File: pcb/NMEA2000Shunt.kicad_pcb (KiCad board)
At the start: 2 copper layers, 87.3 x 28.3 mm, 26 parts, among them IC101 ATTINY3224-SS, K101 Battery, P101 Temp1, P102 Prog, P103 CAN, P105 OLED, U101 MCP2515, U102 TJA1050, U103 NCP1117ST50T3G, U104 INA219-module, X101 8MHz

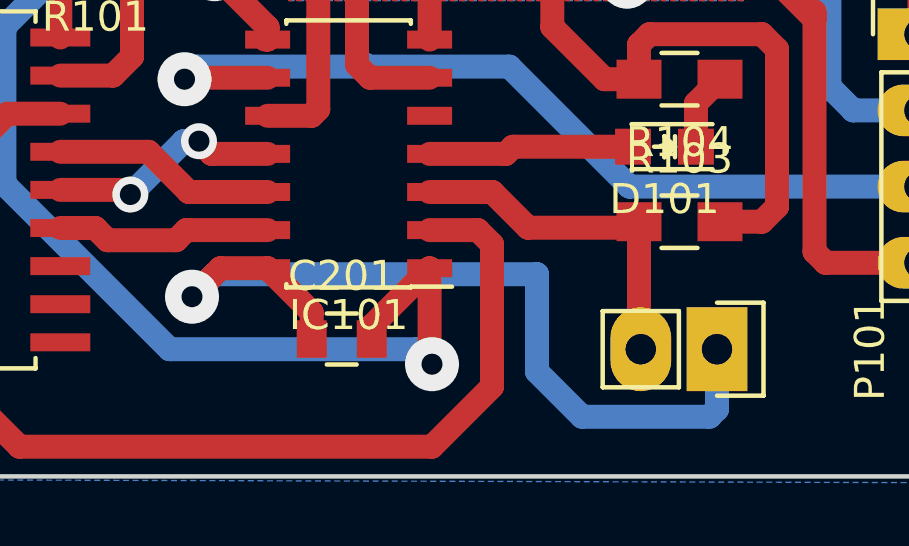
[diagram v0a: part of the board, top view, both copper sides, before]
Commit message: Working version tested with Cansocket and canboat
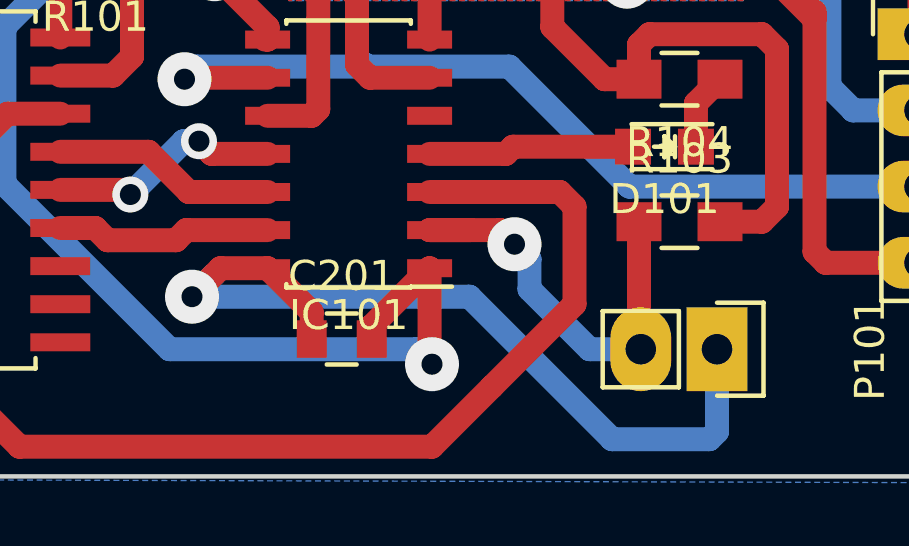
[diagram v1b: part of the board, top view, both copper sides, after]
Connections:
- IC101 pad 2: CANCS -> TEMP1
- IC101 pad 3: TEMP1 -> CANCS
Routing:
- net CANCS: track 37.3 -> 42.5 mm
- net TEMP1: track 11.8 -> 15.8 mm, vias 0 -> 1
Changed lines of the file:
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@@
     (links 65)
     (no_connects 0)
-    (area 105.894999 108.738999 193.365001 137.239001)
+    (area 84.68345 95.464 194.015001 272.896001)
     (thickness 1.6)
     (drawings 12)
-    (tracks 268)
+    (tracks 273)
     (zones 0)
     (modules 26)
@@
       (net 11 5V))
     (pad 2 smd rect (at -2.7 -2.54 180) (size 1.5 0.6) (layers F.Cu F.Paste F.Mask)
+      (net 23 TEMP1))
+    (pad 3 smd rect (at -2.7 -1.27 180) (size 1.5 0.6) (layers F.Cu F.Paste F.Mask)
       (net 3 CANCS))
-    (pad 3 smd rect (at -2.7 -1.27 180) (size 1.5 0.6) (layers F.Cu F.Paste F.Mask)
-      (net 23 TEMP1))
     (pad 4 smd rect (at -2.7 0 180) (size 1.5 0.6) (layers F.Cu F.Paste F.Mask)
       (net 21 LED))
@@
   (segment (start 143.934 127.424) (end 146.56 127.424) (width 0.8) (layer F.Cu) (net 2) (status 20))
   (segment (start 142.594 126.084) (end 143.934 127.424) (width 0.8) (layer F.Cu) (net 2))
-  (segment (start 154.04 131.164) (end 154.04 133.914) (width 0.8) (layer F.Cu) (net 3))
-  (segment (start 153.57 128.694) (end 154.04 129.164) (width 0.8) (layer F.Cu) (net 3))
-  (segment (start 154.04 129.164) (end 154.04 131.164) (width 0.8) (layer F.Cu) (net 3))
-  (segment (start 151.96 128.694) (end 153.57 128.694) (width 0.8) (layer F.Cu) (net 3))
+  (segment (start 151.96 127.424) (end 156.3 127.424) (width 0.8) (layer F.Cu) (net 3) (status 400000))
+  (segment (start 154.04 133.914) (end 152.04 135.914) (width 0.8) (layer F.Cu) (net 3))
+  (segment (start 152.04 135.914) (end 138.29 135.914) (width 0.8) (layer F.Cu) (net 3))
+  (segment (start 138.29 135.914) (end 137.04 134.664) (width 0.8) (layer F.Cu) (net 3))
+  (segment (start 137.04 134.664) (end 137.04 125.664) (width 0.8) (layer F.Cu) (net 3))
+  (segment (start 137.04 125.664) (end 137.89 124.814) (width 0.8) (layer F.Cu) (net 3))
   (segment (start 137.89 124.814) (end 139.65 124.814) (width 0.8) (layer F.Cu) (net 3))
-  (segment (start 137.04 125.664) (end 137.89 124.814) (width 0.8) (layer F.Cu) (net 3))
-  (segment (start 137.04 134.664) (end 137.04 125.664) (width 0.8) (layer F.Cu) (net 3))
-  (segment (start 138.29 135.914) (end 137.04 134.664) (width 0.8) (layer F.Cu) (net 3))
-  (segment (start 152.04 135.914) (end 138.29 135.914) (width 0.8) (layer F.Cu) (net 3))
-  (segment (start 154.04 133.914) (end 152.04 135.914) (width 0.8) (layer F.Cu) (net 3))
+  (segment (start 156.79 131.164) (end 154.04 133.914) (width 0.8) (layer F.Cu) (net 3))
+  (segment (start 156.79 127.914) (end 156.79 131.164) (width 0.8) (layer F.Cu) (net 3))
+  (segment (start 156.3 127.424) (end 156.79 127.914) (width 0.8) (layer F.Cu) (net 3))
+  (segment (start 144.04 130.914) (end 153.29 130.914) (width 0.8) (layer B.Cu) (net 4))
+  (segment (start 161.54 135.414) (end 161.54 132.664) (width 0.8) (layer B.Cu) (net 4) (status 800000))
+  (segment (start 161.29 135.664) (end 161.54 135.414) (width 0.8) (layer B.Cu) (net 4))
+  (segment (start 158.04 135.664) (end 161.29 135.664) (width 0.8) (layer B.Cu) (net 4))
+  (segment (start 153.29 130.914) (end 158.04 135.664) (width 0.8) (layer B.Cu) (net 4))
   (segment (start 174.92 118.854) (end 184.81 118.854) (width 0.8) (layer B.Cu) (net 4))
   (segment (start 184.81 118.854) (end 185.29 119.334) (width 0.8) (layer B.Cu) (net 4))
@@
   (segment (start 165.29 123.914) (end 165.29 119.414) (width 0.8) (layer B.Cu) (net 4))
   (segment (start 166.08 124.704) (end 165.29 123.914) (width 0.8) (layer B.Cu) (net 4))
-  (segment (start 155.54 130.164) (end 155.54 133.414) (width 0.8) (layer B.Cu) (net 4))
   (segment (start 144.99 129.964) (end 144.04 130.914) (width 0.8) (layer F.Cu) (net 4))
   (via (at 144.04 130.914) (size 1.8) (drill 0.7) (layers F.Cu B.Cu) (net 4))
   (segment (start 144.04 130.914) (end 144.79 130.164) (width 0.8) (layer B.Cu) (net 4))
-  (segment (start 144.79 130.164) (end 155.54 130.164) (width 0.8) (layer B.Cu) (net 4))
   (segment (start 146.56 129.964) (end 144.99 129.964) (width 0.8) (layer F.Cu) (net 4))
-  (segment (start 161.54 134.664) (end 161.54 132.664) (width 0.8) (layer B.Cu) (net 4))
-  (segment (start 161.29 134.914) (end 161.54 134.664) (width 0.8) (layer B.Cu) (net 4))
-  (segment (start 157.04 134.914) (end 161.29 134.914) (width 0.8) (layer B.Cu) (net 4))
-  (segment (start 155.54 133.414) (end 157.04 134.914) (width 0.8) (layer B.Cu) (net 4))
   (segment (start 121.29 115.914) (end 121.54 115.914) (width 0.8) (layer F.Cu) (net 4))
   (segment (start 121.54 115.914) (end 122.14 115.314) (width 0.8) (layer F.Cu) (net 4))
@@
   (segment (start 160.83902 125.914) (end 160.83902 124.46498) (width 0.8) (layer F.Cu) (net 22))
   (segment (start 160.83902 124.46498) (end 161.64 123.664) (width 0.8) (layer F.Cu) (net 22))
+  (segment (start 151.96 128.694) (end 154.32 128.694) (width 0.8) (layer F.Cu) (net 23) (status 400000))
+  (segment (start 157.29 132.664) (end 159 132.664) (width 0.8) (layer B.Cu) (net 23) (status 800000))
+  (segment (start 155.29 130.664) (end 157.29 132.664) (width 0.8) (layer B.Cu) (net 23))
+  (segment (start 155.29 129.664) (end 155.29 130.664) (width 0.8) (layer B.Cu) (net 23))
+  (segment (start 154.79 129.164) (end 155.29 129.664) (width 0.8) (layer B.Cu) (net 23))
+  (via (at 154.79 129.164) (size 1.8) (drill 0.7) (layers F.Cu B.Cu) (net 23))
+  (segment (start 154.32 128.694) (end 154.79 129.164) (width 0.8) (layer F.Cu) (net 23))
+  (segment (start 151.96 128.694) (end 153.32 128.694) (width 0.8) (layer F.Cu) (net 23))
+  (segment (start 158.94 129.014) (end 158.94 128.414) (width 0.8) (layer F.Cu) (net 23))
   (segment (start 158.94 128.414) (end 158.94 132.604) (width 0.8) (layer F.Cu) (net 23))
   (segment (start 158.94 132.604) (end 159 132.664) (width 0.8) (layer F.Cu) (net 23))
-  (segment (start 158.739998 128.614002) (end 155.240002 128.614002) (width 0.8) (layer F.Cu) (net 23))
-  (segment (start 154.05 127.424) (end 155.240002 128.614002) (width 0.8) (layer F.Cu) (net 23))
-  (segment (start 154.05 127.424) (end 151.96 127.424) (width 0.8) (layer F.Cu) (net 23))
   (segment (start 158.739998 128.614002) (end 158.94 128.414) (width 0.8) (layer F.Cu) (net 23))
   (segment (start 174.92 126.474) (end 178.48 126.474) (width 0.8) (layer B.Cu) (net 24))
